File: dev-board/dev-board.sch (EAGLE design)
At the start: 44 parts, among them J1 12401832E402A, U1 STM32F103RET6, U2 AT24C64BN-10SU-2.7, U3 FT232RL, U4 MCP2551, U5 Value, X1 8MHz

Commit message: Add leds
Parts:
- added D1, D2: LED_BLUE, LED:CHIP-ROUND-R_0805
- added R15, R16: 10R, Resistor:R_CHIP-0805(2012-METRIC)
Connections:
- removed net PA0: JP2.1, U1A.PA0-WKUP
- new net BOOTLOADER: JP2.1, R16.2, U1A.PA0-WKUP
- new net N$7: D1.A, R15.1
- new net N$8: D2.A, R16.1
- net +3V3: now also R15.2
- net GND: now also D1.C, D2.C
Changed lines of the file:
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@@
 <part name="GND12" library="supply1" library_urn="urn:adsk.eagle:library:371" deviceset="GND" device=""/>
 <part name="C18" library="Capacitor" library_urn="urn:adsk.eagle:library:16290819" deviceset="C" device="CHIP-0805(2012-METRIC)" package3d_urn="urn:adsk.eagle:package:16290897/2" technology="_" value="100nF"/>
+<part name="D1" library="LED" library_urn="urn:adsk.eagle:library:22900745" deviceset="CHIP-ROUND-R" device="_0805" package3d_urn="urn:adsk.eagle:package:24294805/1" value="LED_BLUE"/>
+<part name="D2" library="LED" library_urn="urn:adsk.eagle:library:22900745" deviceset="CHIP-ROUND-R" device="_0805" package3d_urn="urn:adsk.eagle:package:24294805/1" value="LED_BLUE"/>
+<part name="GND25" library="supply1" library_urn="urn:adsk.eagle:library:371" deviceset="GND" device=""/>
+<part name="R15" library="Resistor" library_urn="urn:adsk.eagle:library:16378527" deviceset="R" device="CHIP-0805(2012-METRIC)" package3d_urn="urn:adsk.eagle:package:16378559/2" technology="_" value="10R"/>
+<part name="R16" library="Resistor" library_urn="urn:adsk.eagle:library:16378527" deviceset="R" device="CHIP-0805(2012-METRIC)" package3d_urn="urn:adsk.eagle:package:16378559/2" technology="_" value="10R"/>
+<part name="+3V10" library="supply1" library_urn="urn:adsk.eagle:library:371" deviceset="+3V3" device=""/>
 </parts>
 <sheets>
@@
 <attribute name="NAME" x="-63.5" y="-63.5" size="1.778" layer="95"/>
 <attribute name="VALUE" x="-63.5" y="-66.04" size="1.778" layer="96"/>
+</instance>
+<instance part="D1" gate="G$1" x="-144.78" y="101.6" smashed="yes">
+<attribute name="NAME" x="-142.24" y="100.838" size="1.778" layer="95" rot="R180" align="top-right"/>
+<attribute name="VALUE" x="-142.24" y="98.298" size="1.778" layer="96" rot="R180" align="top-right"/>
+</instance>
+<instance part="D2" gate="G$1" x="-124.46" y="101.6" smashed="yes">
+<attribute name="NAME" x="-121.92" y="100.838" size="1.778" layer="95" rot="R180" align="top-right"/>
+<attribute name="VALUE" x="-121.92" y="98.298" size="1.778" layer="96" rot="R180" align="top-right"/>
+</instance>
+<instance part="GND25" gate="1" x="-144.78" y="88.9" smashed="yes">
+<attribute name="VALUE" x="-147.32" y="86.36" size="1.778" layer="96"/>
+</instance>
+<instance part="R15" gate="G$1" x="-144.78" y="114.3" smashed="yes" rot="R90">
+<attribute name="NAME" x="-147.32" y="114.3" size="1.778" layer="95" rot="R90" align="center"/>
+<attribute name="VALUE" x="-142.24" y="114.3" size="1.778" layer="95" rot="R90" align="center"/>
+</instance>
+<instance part="R16" gate="G$1" x="-124.46" y="114.3" smashed="yes" rot="R90">
+<attribute name="NAME" x="-127" y="114.3" size="1.778" layer="95" rot="R90" align="center"/>
+<attribute name="VALUE" x="-121.92" y="114.3" size="1.778" layer="95" rot="R90" align="center"/>
+</instance>
+<instance part="+3V10" gate="G$1" x="-144.78" y="127" smashed="yes">
+<attribute name="VALUE" x="-147.32" y="121.92" size="1.778" layer="96" rot="R90"/>
 </instance>
 </instances>
@@
 <wire x1="-33.02" y1="-76.2" x2="-27.94" y2="-76.2" width="0.1524" layer="91"/>
 </segment>
+<segment>
+<pinref part="+3V10" gate="G$1" pin="+3V3"/>
+<pinref part="R15" gate="G$1" pin="2"/>
+<wire x1="-144.78" y1="124.46" x2="-144.78" y2="119.38" width="0.1524" layer="91"/>
+</segment>
 </net>
 <net name="N$1" class="0">
@@
 <pinref part="GND28" gate="1" pin="GND"/>
 </segment>
+<segment>
+<pinref part="D1" gate="G$1" pin="C"/>
+<pinref part="GND25" gate="1" pin="GND"/>
+<wire x1="-144.78" y1="91.44" x2="-144.78" y2="96.52" width="0.1524" layer="91"/>
+<pinref part="D2" gate="G$1" pin="C"/>
+<wire x1="-144.78" y1="96.52" x2="-124.46" y2="96.52" width="0.1524" layer="91"/>
+<junction x="-144.78" y="96.52"/>
+</segment>
 </net>
 <net name="N$13" class="0">
@@
 </segment>
 </net>
-<net name="PA0" class="0">
+<net name="BOOTLOADER" class="0">
 <segment>
 <pinref part="U1" gate="A" pin="PA0-WKUP"/>
@@
 <wire x1="-5.08" y1="119.38" x2="-10.16" y2="119.38" width="0.1524" layer="91"/>
 <label x="-10.16" y="119.38" size="0.8128" layer="95" rot="R180" xref="yes"/>
+</segment>
+<segment>
+<pinref part="R16" gate="G$1" pin="2"/>
+<wire x1="-124.46" y1="119.38" x2="-124.46" y2="121.92" width="0.1524" layer="91"/>
+<wire x1="-124.46" y1="121.92" x2="-119.38" y2="121.92" width="0.1524" layer="91"/>
+<label x="-119.38" y="121.92" size="1.778" layer="95" xref="yes"/>
 </segment>
 </net>
@@
 </segment>
 </net>
+<net name="N$7" class="0">
+<segment>
+<pinref part="R15" gate="G$1" pin="1"/>
+<pinref part="D1" gate="G$1" pin="A"/>
+<wire x1="-144.78" y1="109.22" x2="-144.78" y2="104.14" width="0.1524" layer="91"/>
+</segment>
+</net>
+<net name="N$8" class="0">
+<segment>
+<pinref part="R16" gate="G$1" pin="1"/>
+<pinref part="D2" gate="G$1" pin="A"/>
+<wire x1="-124.46" y1="109.22" x2="-124.46" y2="104.14" width="0.1524" layer="91"/>
+</segment>
+</net>

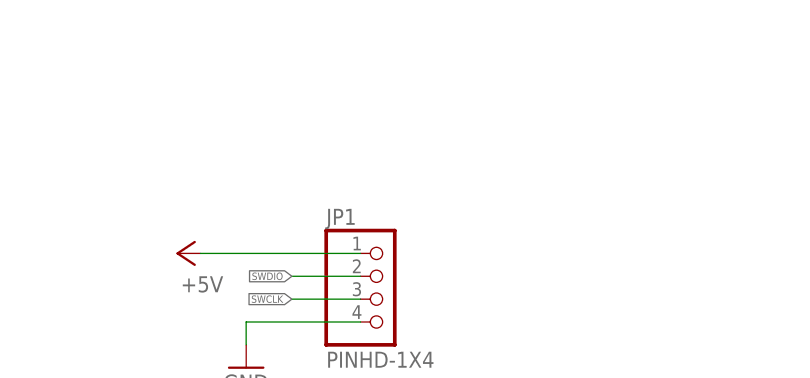
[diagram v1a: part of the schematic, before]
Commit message: Add breakout for various voltages
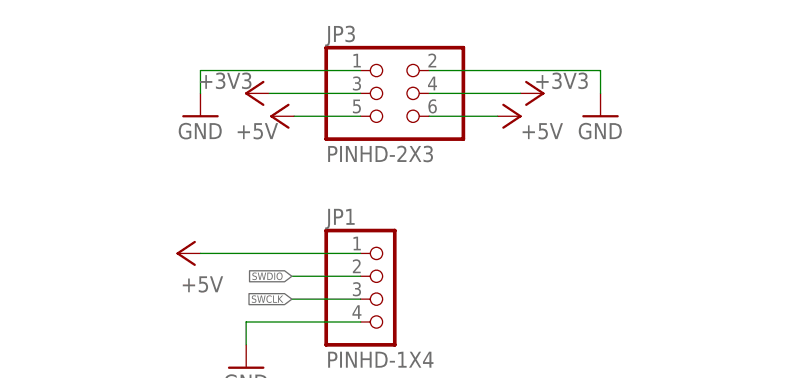
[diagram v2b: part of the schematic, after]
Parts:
- added JP3: PINHD-2X3, Connector:PINHD-2X3
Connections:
- net +3V3: now also JP3.3, JP3.4
- net +5V: now also JP3.5, JP3.6
- net GND: now also JP3.1, JP3.2
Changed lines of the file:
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@@
 <part name="R16" library="Resistor" library_urn="urn:adsk.eagle:library:16378527" deviceset="R" device="CHIP-0805(2012-METRIC)" package3d_urn="urn:adsk.eagle:package:16378559/2" technology="_" value="10R"/>
 <part name="+3V10" library="supply1" library_urn="urn:adsk.eagle:library:371" deviceset="+3V3" device=""/>
+<part name="JP3" library="Connector" library_urn="urn:adsk.eagle:library:16378166" deviceset="PINHD-2X3" device="" package3d_urn="urn:adsk.eagle:package:22462/2"/>
+<part name="P+5" library="supply1" library_urn="urn:adsk.eagle:library:371" deviceset="+5V" device=""/>
+<part name="P+9" library="supply1" library_urn="urn:adsk.eagle:library:371" deviceset="+5V" device=""/>
+<part name="GND29" library="supply1" library_urn="urn:adsk.eagle:library:371" deviceset="GND" device=""/>
+<part name="GND30" library="supply1" library_urn="urn:adsk.eagle:library:371" deviceset="GND" device=""/>
+<part name="+3V11" library="supply1" library_urn="urn:adsk.eagle:library:371" deviceset="+3V3" device=""/>
+<part name="+3V12" library="supply1" library_urn="urn:adsk.eagle:library:371" deviceset="+3V3" device=""/>
 </parts>
 <sheets>
@@
 <instance part="+3V10" gate="G$1" x="-144.78" y="127" smashed="yes">
 <attribute name="VALUE" x="-147.32" y="121.92" size="1.778" layer="96" rot="R90"/>
+</instance>
+<instance part="JP3" gate="A" x="-2.54" y="157.48" smashed="yes">
+<attribute name="NAME" x="-8.89" y="163.195" size="1.778" layer="95"/>
+<attribute name="VALUE" x="-8.89" y="149.86" size="1.778" layer="96"/>
+</instance>
+<instance part="P+5" gate="1" x="-14.986" y="154.94" smashed="yes" rot="R90">
+<attribute name="VALUE" x="-14.224" y="154.178" size="1.778" layer="96" rot="R180"/>
+</instance>
+<instance part="P+9" gate="1" x="12.7" y="154.94" smashed="yes" rot="R270">
+<attribute name="VALUE" x="12.7" y="152.4" size="1.778" layer="96"/>
+</instance>
+<instance part="GND29" gate="1" x="-22.86" y="154.94" smashed="yes">
+<attribute name="VALUE" x="-25.4" y="152.4" size="1.778" layer="96"/>
+</instance>
+<instance part="GND30" gate="1" x="21.59" y="154.94" smashed="yes">
+<attribute name="VALUE" x="19.05" y="152.4" size="1.778" layer="96"/>
+</instance>
+<instance part="+3V11" gate="G$1" x="15.24" y="157.48" smashed="yes" rot="R270">
+<attribute name="VALUE" x="14.224" y="157.988" size="1.778" layer="96"/>
+</instance>
+<instance part="+3V12" gate="G$1" x="-17.78" y="157.48" smashed="yes" rot="R90">
+<attribute name="VALUE" x="-17.018" y="159.766" size="1.778" layer="96" rot="R180"/>
 </instance>
 </instances>
@@
 <wire x1="-144.78" y1="124.46" x2="-144.78" y2="119.38" width="0.1524" layer="91"/>
 </segment>
+<segment>
+<pinref part="JP3" gate="A" pin="3"/>
+<wire x1="-5.08" y1="157.48" x2="-15.24" y2="157.48" width="0.1524" layer="91"/>
+<pinref part="+3V12" gate="G$1" pin="+3V3"/>
+</segment>
+<segment>
+<pinref part="JP3" gate="A" pin="4"/>
+<wire x1="2.54" y1="157.48" x2="12.7" y2="157.48" width="0.1524" layer="91"/>
+<pinref part="+3V11" gate="G$1" pin="+3V3"/>
+</segment>
 </net>
 <net name="N$1" class="0">
@@
 <wire x1="96.52" y1="-10.16" x2="101.6" y2="-10.16" width="0.1524" layer="91"/>
 <junction x="96.52" y="-10.16"/>
+</segment>
+<segment>
+<pinref part="JP3" gate="A" pin="5"/>
+<wire x1="-5.08" y1="154.94" x2="-12.446" y2="154.94" width="0.1524" layer="91"/>
+<pinref part="P+5" gate="1" pin="+5V"/>
+</segment>
+<segment>
+<pinref part="JP3" gate="A" pin="6"/>
+<wire x1="2.54" y1="154.94" x2="10.16" y2="154.94" width="0.1524" layer="91"/>
+<pinref part="P+9" gate="1" pin="+5V"/>
 </segment>
 </net>
@@
 <junction x="-144.78" y="96.52"/>
 </segment>
-</net>
+<segment>
+<pinref part="GND29" gate="1" pin="GND"/>
+<wire x1="-22.86" y1="157.48" x2="-22.86" y2="160.02" width="0.1524" layer="91"/>
+<pinref part="JP3" gate="A" pin="1"/>
+<wire x1="-22.86" y1="160.02" x2="-5.08" y2="160.02" width="0.1524" layer="91"/>
+</segment>
+<segment>
+<pinref part="JP3" gate="A" pin="2"/>
+<wire x1="2.54" y1="160.02" x2="21.59" y2="160.02" width="0.1524" layer="91"/>
+<pinref part="GND30" gate="1" pin="GND"/>
+<wire x1="21.59" y1="160.02" x2="21.59" y2="157.48" width="0.1524" layer="91"/>
+</segment>
+</net>
